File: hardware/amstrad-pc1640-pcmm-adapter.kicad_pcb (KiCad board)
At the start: 2 copper layers, 80 x 45 mm, 8 parts, among them J1 DB9_Male, J2 DIN-8, J3 +5V/GND, U1 74HC04, U2 74HC86

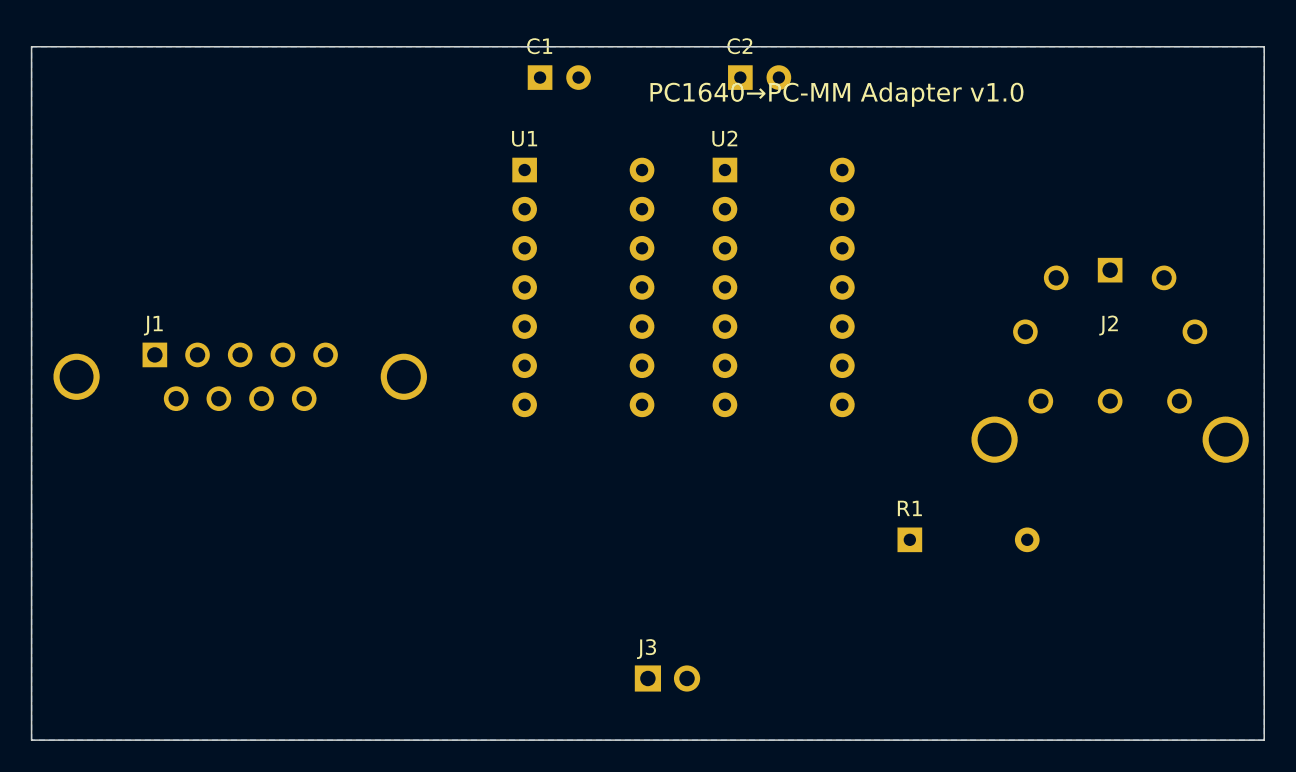
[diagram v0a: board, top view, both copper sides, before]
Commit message: Complete PCB routing and generate manufacturing files
Freerouting auto-routed all nets in 5 passes (0.85s), 0 unrouted.
DRC passed: 0 critical errors, 0 unconnected items, 1 cosmetic warning.

Generated outputs:
- Routed PCB with GND copper pour on B.Cu
- Gerber files (F.Cu, B.Cu, silkscreen, mask, edge cuts, drill)
- Manufacturing-ready zip for JLCPCB/PCBWay
- GenCAD export for BOM tools
- Specctra DSN/SES files

Co-Authored-By: Claude Opus 4.6 <noreply@anthropic.com>
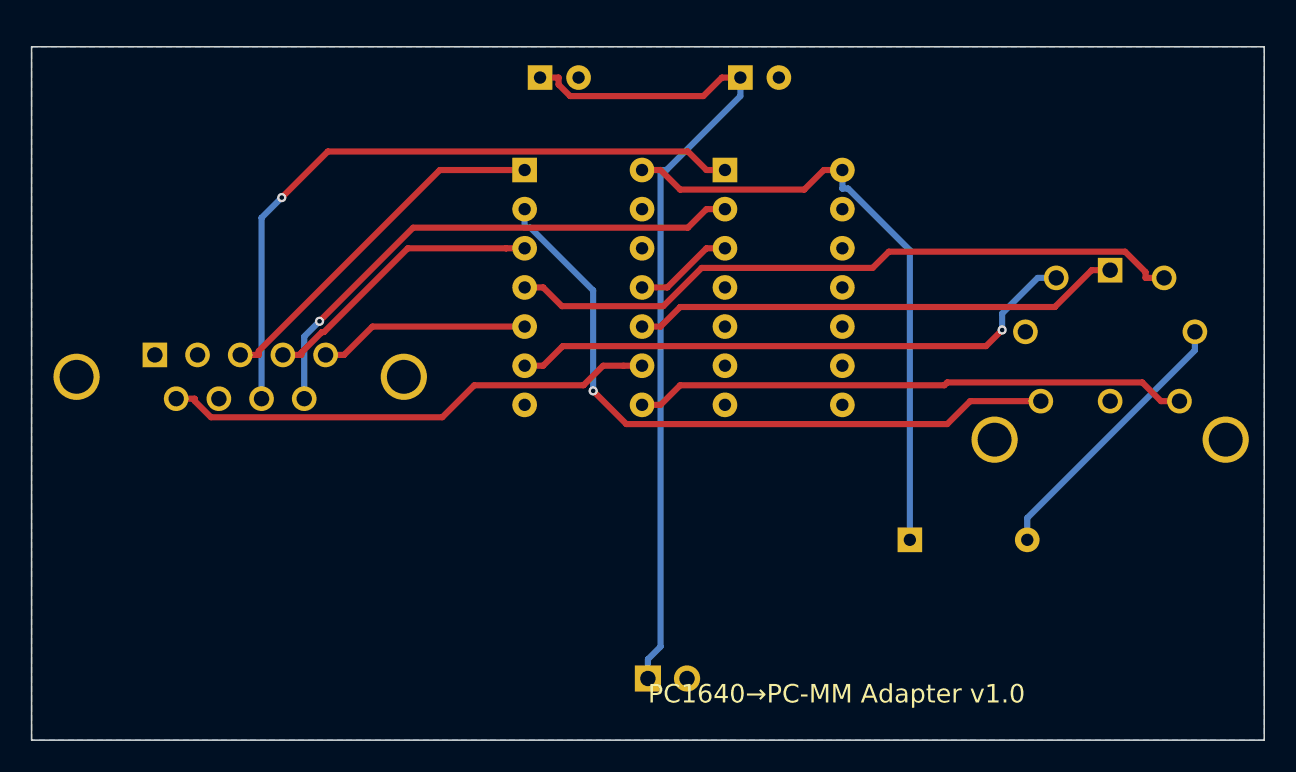
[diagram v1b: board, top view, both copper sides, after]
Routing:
- net +5V: track 0.00 -> 97.3 mm
- net RED_INV: track 0.00 -> 44.4 mm, vias 0 -> 1
- net GREEN_INV: track 0.00 -> 44.4 mm
- net HSYNC: track 0.00 -> 44.1 mm, vias 0 -> 1
- net BLUE_INV: track 0.00 -> 37.5 mm, vias 0 -> 1
- net INTENSITY_INV: track 0.00 -> 36.0 mm
- net VSYNC: track 0.00 -> 34.8 mm, vias 0 -> 1
- net INTENSITY: track 0.00 -> 32.2 mm
- net CSYNC_INV: track 0.00 -> 31.9 mm
- net RED: track 0.00 -> 23.6 mm
- net GREEN: track 0.00 -> 18.6 mm
- net BLACK: track 0.00 -> 18.0 mm
- net BLUE: track 0.00 -> 13.7 mm
- net CSYNC: track 0.00 -> 6.43 mm

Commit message: Reduce PCB from 80x45mm to 80x32mm by moving J3 and R1 up
Moved J3 (+5V/GND header) from y=121 to y=108 (below ICs) and
R1 from (157,112) to (150,108). Board height reduced 29%.
All nets routed, DRC passed.

Co-Authored-By: Claude Opus 4.6 <noreply@anthropic.com>
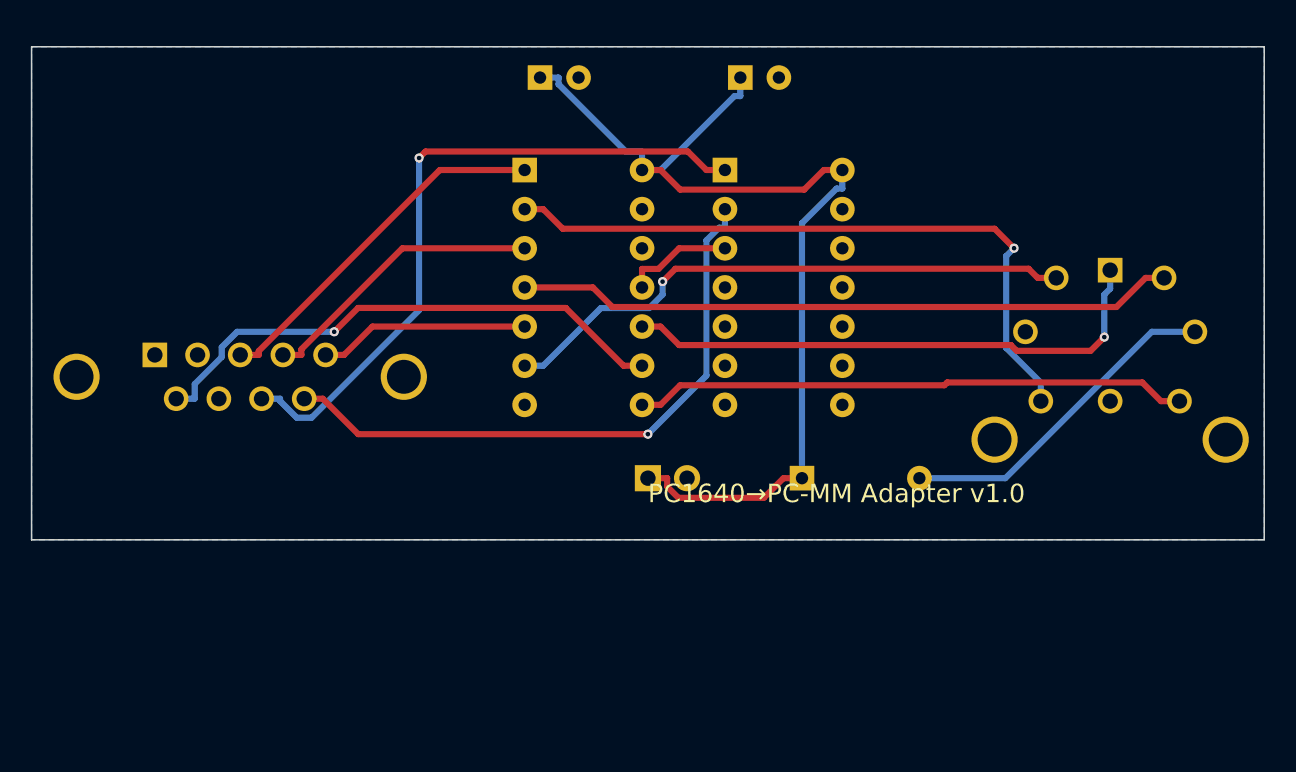
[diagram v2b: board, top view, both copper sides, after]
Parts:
- moved J3 13.0 mm to (140.0, 108.0)
- moved R1 8.06 mm to (150.0, 108.0)
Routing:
- net +5V: track 97.3 -> 66.4 mm
- net VSYNC: track 34.8 -> 40.2 mm
- net BLACK: track 18.0 -> 21.8 mm
- net CSYNC_INV: track 31.9 -> 35.5 mm, vias 0 -> 1
- net INTENSITY: track 32.2 -> 35.2 mm, vias 0 -> 1
- net GREEN_INV: track 44.4 -> 42.8 mm
- net CSYNC: track 6.43 -> 7.14 mm
- net RED_INV: track 44.4 -> 43.9 mm
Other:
- board size 80 x 45 mm -> 80 x 32 mm

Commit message: Add 3D model references and render PCB with components
Added 3D model paths (DIP-14, DE-9, capacitors, resistor, pin header)
to generate-pcb.py footprints. Rendered via GLB export + pyrender since
kicad-cli render doesn't load 3D models on macOS. DIN-8 connector has
no standard KiCad 3D model.

Co-Authored-By: Claude Opus 4.6 <noreply@anthropic.com>
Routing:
- net +5V: track 66.4 -> 0.00 mm
- net HSYNC: track 44.1 -> 0.00 mm, vias 1 -> 0
- net RED_INV: track 43.9 -> 0.00 mm, vias 1 -> 0
- net GREEN_INV: track 42.8 -> 0.00 mm
- net VSYNC: track 40.2 -> 0.00 mm, vias 1 -> 0
- net BLUE_INV: track 37.8 -> 0.00 mm, vias 1 -> 0
- net INTENSITY_INV: track 36.0 -> 0.00 mm
- net CSYNC_INV: track 35.5 -> 0.00 mm, vias 1 -> 0
- net INTENSITY: track 35.2 -> 0.00 mm, vias 1 -> 0
- net RED: track 23.6 -> 0.00 mm
- net BLACK: track 21.8 -> 0.00 mm
- net GREEN: track 18.8 -> 0.00 mm
- net BLUE: track 13.7 -> 0.00 mm
- net CSYNC: track 7.14 -> 0.00 mm
